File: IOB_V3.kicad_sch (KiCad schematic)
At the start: 9 parts, among them J1 Conn_01x02, J18 Conn_01x10, J2 Conn_01x03, J20 Conn_01x10, U1 REF3033

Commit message: Layer change + INA change + SPI 24V added + minor changes
Stitching is still missing
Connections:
- net +24V: now also J18.9 (Pin_9), J20.9 (Pin_9)
- no-connect marks 4 -> 2

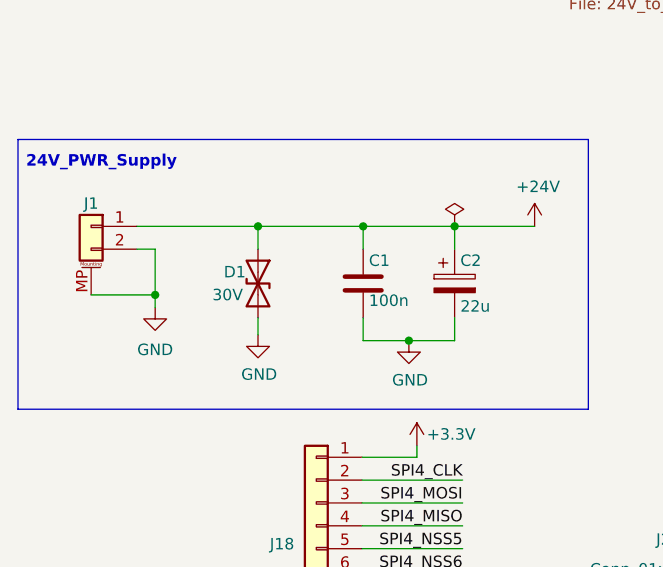
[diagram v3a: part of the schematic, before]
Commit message: Changed 5V Plane to 3.3V Changed INA350 Supply to 3.3V Minor tweaks
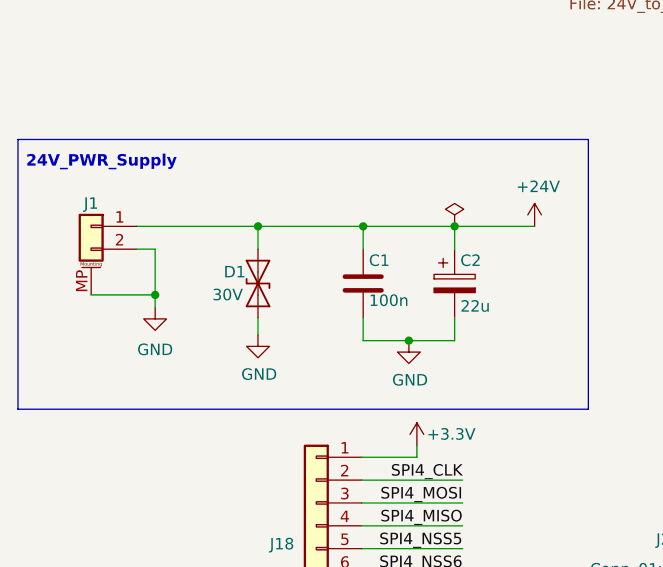
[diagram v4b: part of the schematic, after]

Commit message: Fixed Lib Mess
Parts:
- C2: symbol IOB-rescue:CP-Device -> Device:CP
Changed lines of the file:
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@@
     (pin "1")
   )
-  (symbol (lib_id "IOB-rescue:CP-Device") (at 91.821 147.828 0) (unit 1)
+  (symbol (lib_id "Device:CP") (at 91.821 147.828 0) (unit 1)
     (in_bom yes) (on_board yes)
     (property "Reference" "C2" (id 0) (at 92.456 145.288 0)
@@
     )
     (path "/e7136250-cee6-4520-acb7-2950e0829e43/7426b94e-ffc2-452e-843f-c6ffae4705a2/7f7da753-6b52-4899-b7f4-dfbe24200742"
-      (reference "IC1") (unit 1) (value "PINA350ABSIDDFR") (footprint "KiCad:SOT65P280X110-8N")
+      (reference "IC1") (unit 1) (value "PINA350ABSIDDFR") (footprint "SOT65P280X110-8N")
     )
     (path "/e7136250-cee6-4520-acb7-2950e0829e43/95b5f669-3e5e-48d4-8512-b857a5d5915c/7f7da753-6b52-4899-b7f4-dfbe24200742"
-      (reference "IC2") (unit 1) (value "PINA350ABSIDDFR") (footprint "KiCad:SOT65P280X110-8N")
+      (reference "IC2") (unit 1) (value "PINA350ABSIDDFR") (footprint "SOT65P280X110-8N")
     )
     (path "/e7136250-cee6-4520-acb7-2950e0829e43/a958e3f8-bd63-42b2-ac9a-4ffad0a91676/7f7da753-6b52-4899-b7f4-dfbe24200742"
-      (reference "IC3") (unit 1) (value "PINA350ABSIDDFR") (footprint "KiCad:SOT65P280X110-8N")
+      (reference "IC3") (unit 1) (value "PINA350ABSIDDFR") (footprint "SOT65P280X110-8N")
     )
     (path "/e7136250-cee6-4520-acb7-2950e0829e43/7ea1ea46-2b35-49b1-a809-dcbd86e73c96/7f7da753-6b52-4899-b7f4-dfbe24200742"
-      (reference "IC4") (unit 1) (value "PINA350ABSIDDFR") (footprint "KiCad:SOT65P280X110-8N")
+      (reference "IC4") (unit 1) (value "PINA350ABSIDDFR") (footprint "SOT65P280X110-8N")
     )
     (path "/e7136250-cee6-4520-acb7-2950e0829e43/c637b127-297c-4e8f-be4e-b918078086bf/7f7da753-6b52-4899-b7f4-dfbe24200742"
-      (reference "IC5") (unit 1) (value "PINA350ABSIDDFR") (footprint "KiCad:SOT65P280X110-8N")
+      (reference "IC5") (unit 1) (value "PINA350ABSIDDFR") (footprint "SOT65P280X110-8N")
     )
     (path "/e7136250-cee6-4520-acb7-2950e0829e43/82164960-bf22-4200-8575-df11cb483928/7f7da753-6b52-4899-b7f4-dfbe24200742"
-      (reference "IC6") (unit 1) (value "PINA350ABSIDDFR") (footprint "KiCad:SOT65P280X110-8N")
+      (reference "IC6") (unit 1) (value "PINA350ABSIDDFR") (footprint "SOT65P280X110-8N")
     )
     (path "/e7136250-cee6-4520-acb7-2950e0829e43/8b85e5f6-8968-4f47-ad1c-3423d27b22c2/7f7da753-6b52-4899-b7f4-dfbe24200742"
-      (reference "IC7") (unit 1) (value "PINA350ABSIDDFR") (footprint "KiCad:SOT65P280X110-8N")
+      (reference "IC7") (unit 1) (value "PINA350ABSIDDFR") (footprint "SOT65P280X110-8N")
     )
     (path "/e7136250-cee6-4520-acb7-2950e0829e43/1cfeda7b-3d15-40f9-ac91-2926e2fcb9b6/7f7da753-6b52-4899-b7f4-dfbe24200742"
-      (reference "IC8") (unit 1) (value "PINA350ABSIDDFR") (footprint "KiCad:SOT65P280X110-8N")
+      (reference "IC8") (unit 1) (value "PINA350ABSIDDFR") (footprint "SOT65P280X110-8N")
     )
     (path "/e7136250-cee6-4520-acb7-2950e0829e43/ca909406-9a8c-443a-8a4f-137543955aa7/7f7da753-6b52-4899-b7f4-dfbe24200742"
-      (reference "IC9") (unit 1) (value "PINA350ABSIDDFR") (footprint "KiCad:SOT65P280X110-8N")
+      (reference "IC9") (unit 1) (value "PINA350ABSIDDFR") (footprint "SOT65P280X110-8N")
     )
     (path "/e7136250-cee6-4520-acb7-2950e0829e43/e315361b-ca51-47cd-85fc-82009ac7ddee/7f7da753-6b52-4899-b7f4-dfbe24200742"
-      (reference "IC10") (unit 1) (value "PINA350ABSIDDFR") (footprint "KiCad:SOT65P280X110-8N")
+      (reference "IC10") (unit 1) (value "PINA350ABSIDDFR") (footprint "SOT65P280X110-8N")
     )
     (path "/e7136250-cee6-4520-acb7-2950e0829e43/2c710a03-064f-48b6-8156-1ab0fa7c8290/7f7da753-6b52-4899-b7f4-dfbe24200742"
-      (reference "IC11") (unit 1) (value "PINA350ABSIDDFR") (footprint "KiCad:SOT65P280X110-8N")
+      (reference "IC11") (unit 1) (value "PINA350ABSIDDFR") (footprint "SOT65P280X110-8N")
     )
     (path "/e7136250-cee6-4520-acb7-2950e0829e43/7baf78c5-b11e-457b-812f-beadef1c4ebe/7f7da753-6b52-4899-b7f4-dfbe24200742"
-      (reference "IC12") (unit 1) (value "PINA350ABSIDDFR") (footprint "KiCad:SOT65P280X110-8N")
+      (reference "IC12") (unit 1) (value "PINA350ABSIDDFR") (footprint "SOT65P280X110-8N")
     )
     (path "/3bbae5d4-6082-49cc-a334-20e15dfcb8e0"
@@
     )
     (path "/33332500-4da3-42ef-9bb3-bc804f9ab4ce/97310e5b-8905-40d9-aa0f-4f4327e46ba1"
-      (reference "U14") (unit 1) (value "TS30041") (footprint "Package_DFN_QFN:QFN-16-1EP_3x3mm_P0.5mm_EP1.9x1.9mm_ThermalVias")
+      (reference "U14") (unit 1) (value "TS30041") (footprint "Package_DFN_QFN:QFN-16-1EP_3x3mm_P0.5mm_EP1.75x1.75mm_ThermalVias")
     )
     (path "/534d7b1f-d272-47da-b7a1-47aab2c48175/5021d1de-11ed-4d90-b4d1-82380f2e5e51"
@@
     )
     (path "/534d7b1f-d272-47da-b7a1-47aab2c48175/dd589c3e-1a73-40e3-b0dc-96c44ecf7431"
-      (reference "U19") (unit 1) (value "STM32G474MET3") (footprint "STM32:STM32G474MET3")
+      (reference "U19") (unit 1) (value "STM32G474MET3") (footprint "Package_QFP:LQFP-80_12x12mm_P0.5mm")
     )
     (path "/534d7b1f-d272-47da-b7a1-47aab2c48175/23c64707-1071-4233-bd99-9a271bd42b6f"
